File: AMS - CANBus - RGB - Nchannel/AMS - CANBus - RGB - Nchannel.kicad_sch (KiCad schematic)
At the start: 17 parts, among them J1 Power_And_CAN, J2 Screw_Terminal_01x05, Q1 IRF9Z34NPBF, Q10 2N7002, U1 LTV-817, U5 3568

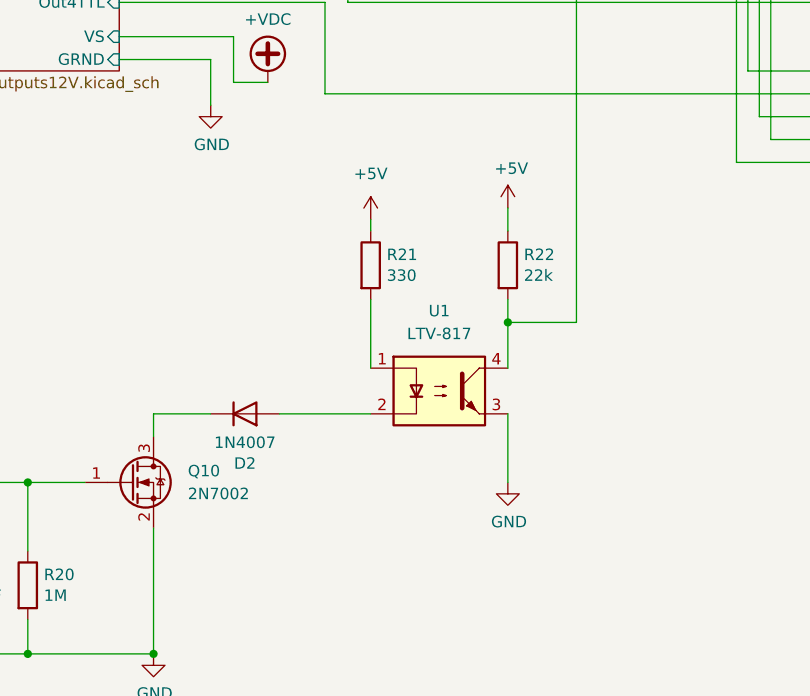
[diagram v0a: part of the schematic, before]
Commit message: RGB - Nchannel done and routed. V1.0 Rev A
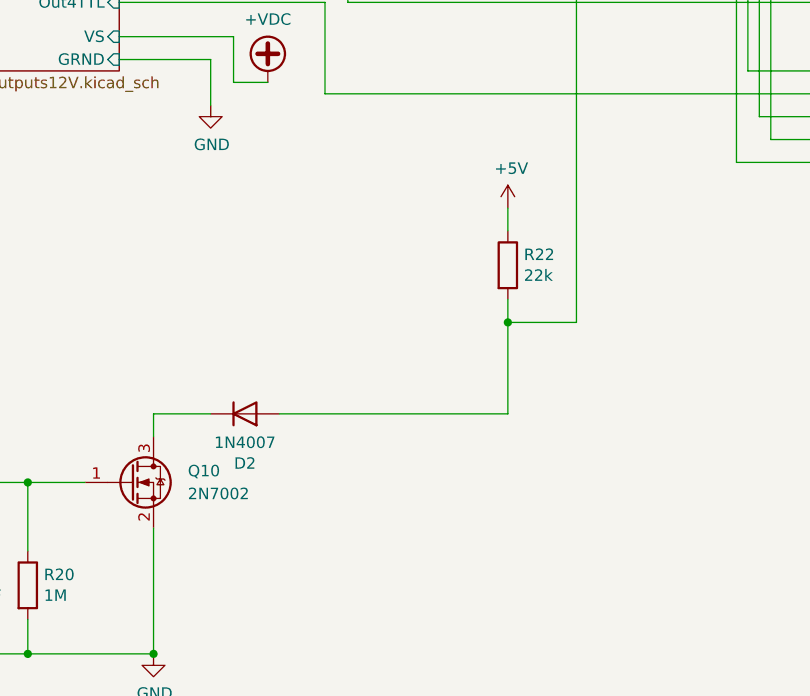
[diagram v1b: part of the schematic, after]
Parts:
- removed R21: 330, Resistor_SMD:R_1206_3216Metric_Pad1.30x1.75mm_HandSolder, symbol Device:R
- removed U1: LTV-817, Package_DIP:DIP-4_W7.62mm, symbol Isolator:LTV-817
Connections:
- net BareMinAtmel328P/PD4-D4: now also D2.2 (A)

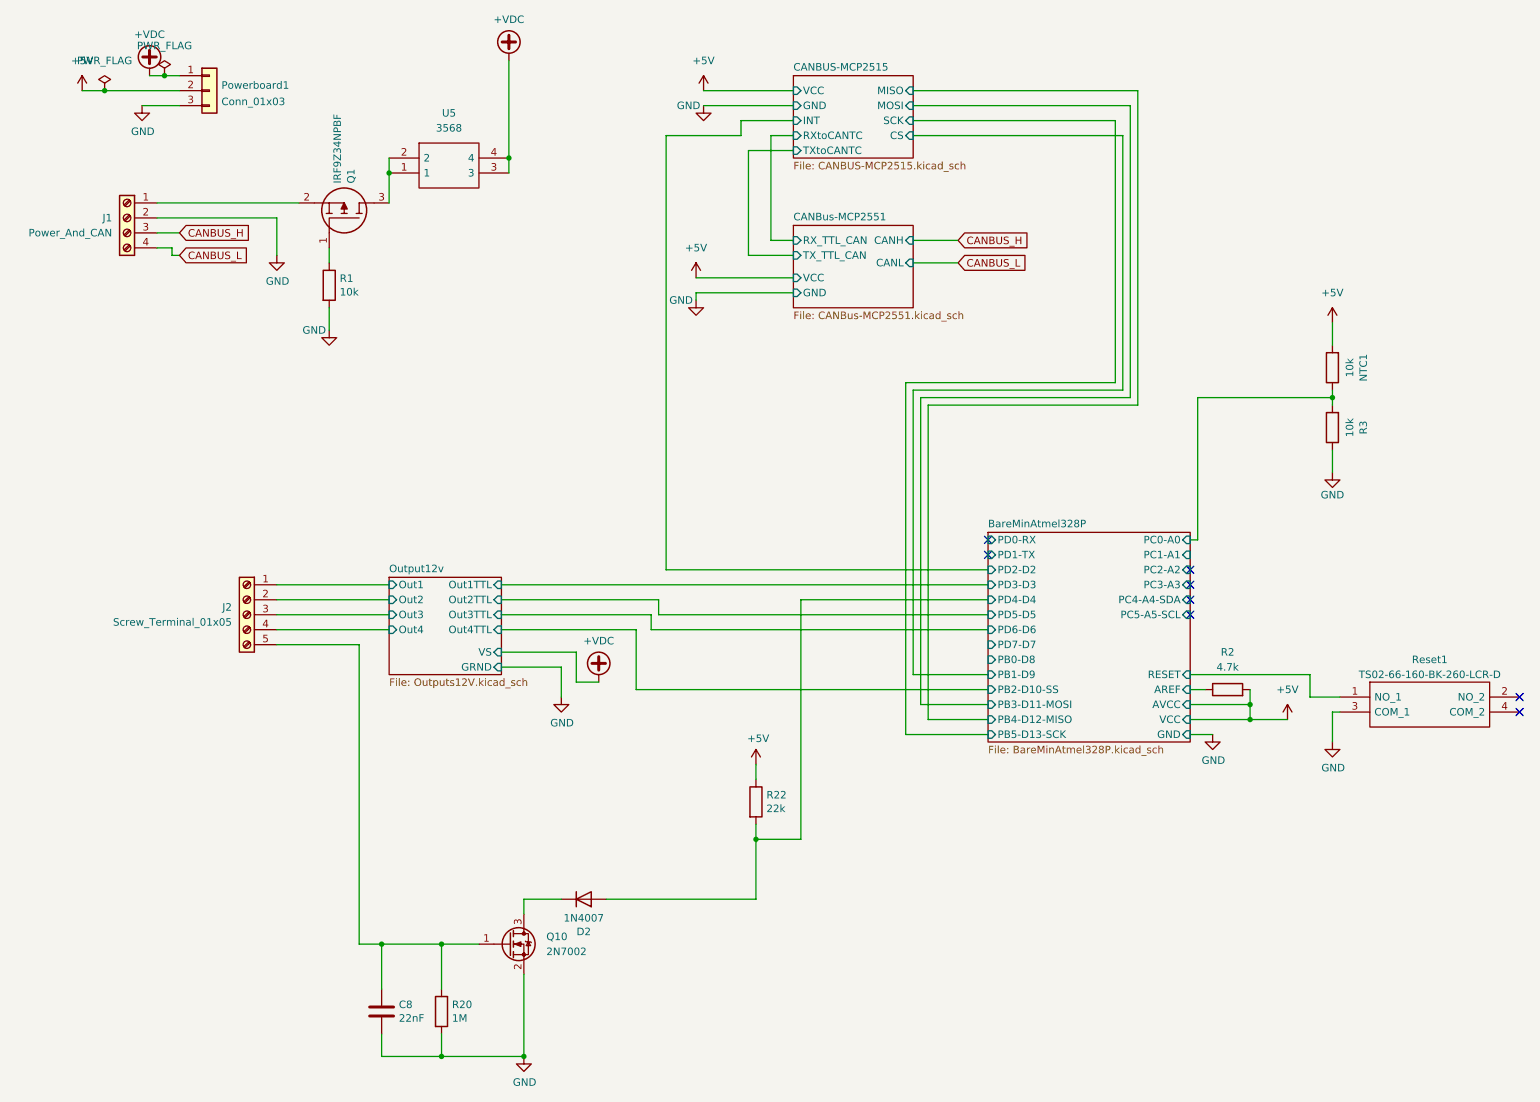
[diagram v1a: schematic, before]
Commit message: routing and stuff are fixed along with the addition of the I2c bus being pulled out.
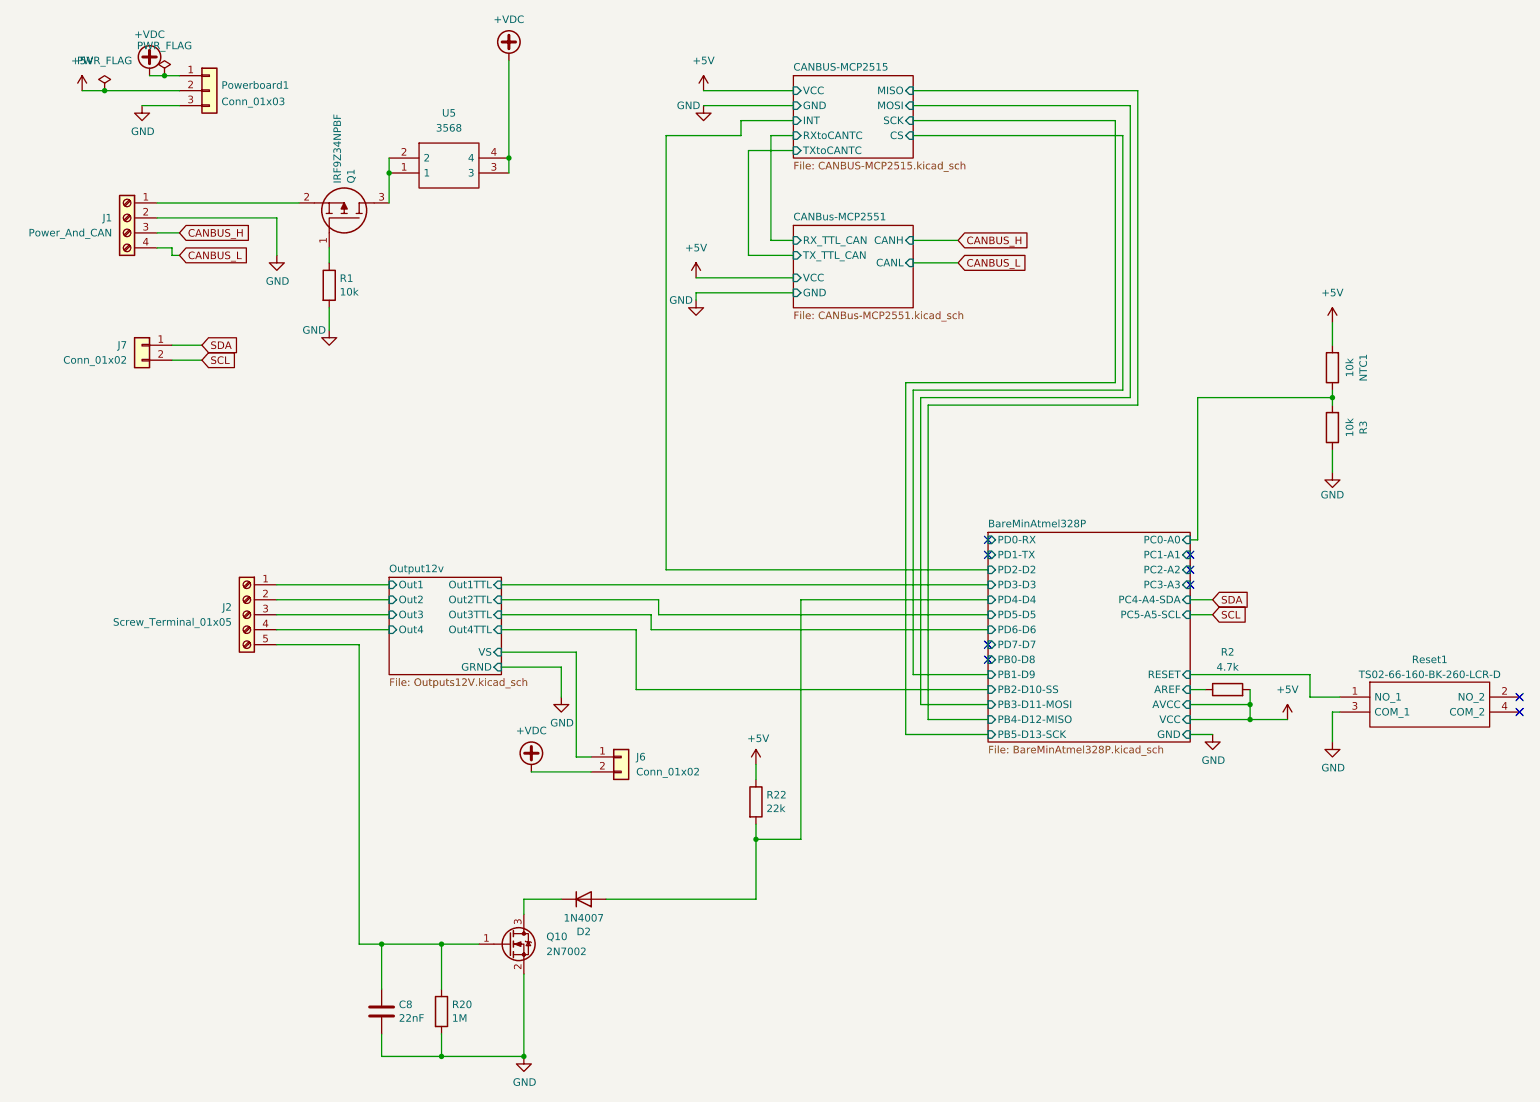
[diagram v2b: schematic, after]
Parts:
- added J6, J7: Conn_01x02, Connector_PinHeader_2.54mm:PinHeader_1x02_P2.54mm_Vertical, symbol Connector_Generic:Conn_01x02
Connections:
- net +VDC: now also J6.2 (Pin_2)
- new net Output12v/VS: J6.1 (Pin_1)
- new net SCL: J7.2 (Pin_2)
- new net SDA: J7.1 (Pin_1)
- no-connect marks 8 -> 9
